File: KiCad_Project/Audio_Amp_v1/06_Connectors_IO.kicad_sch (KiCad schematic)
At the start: 0 parts

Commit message: Updated Power management section, Bluetooth receiver and connectors. Added some components footprints and 3D.
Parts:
- added J1: TS-103-T-A, TS_103_T_A:SAMTEC_TS-103-T-A, symbol TS-103-T-A:TS-103-T-A
- added U2: 2137160001, 2137160001_MOL, symbol USB_C:2137160001
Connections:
- new net: U2.A1 (GND), U2.A12 (GND), U2.B1 (GND), U2.B12 (GND)
- new net: U2.A4 (VBUS), U2.A9 (VBUS), U2.B4 (VBUS), U2.B9 (VBUS)
- new net GNDA: J1.03
- new net UART_RX: J1.02
- new net UART_TX: J1.01

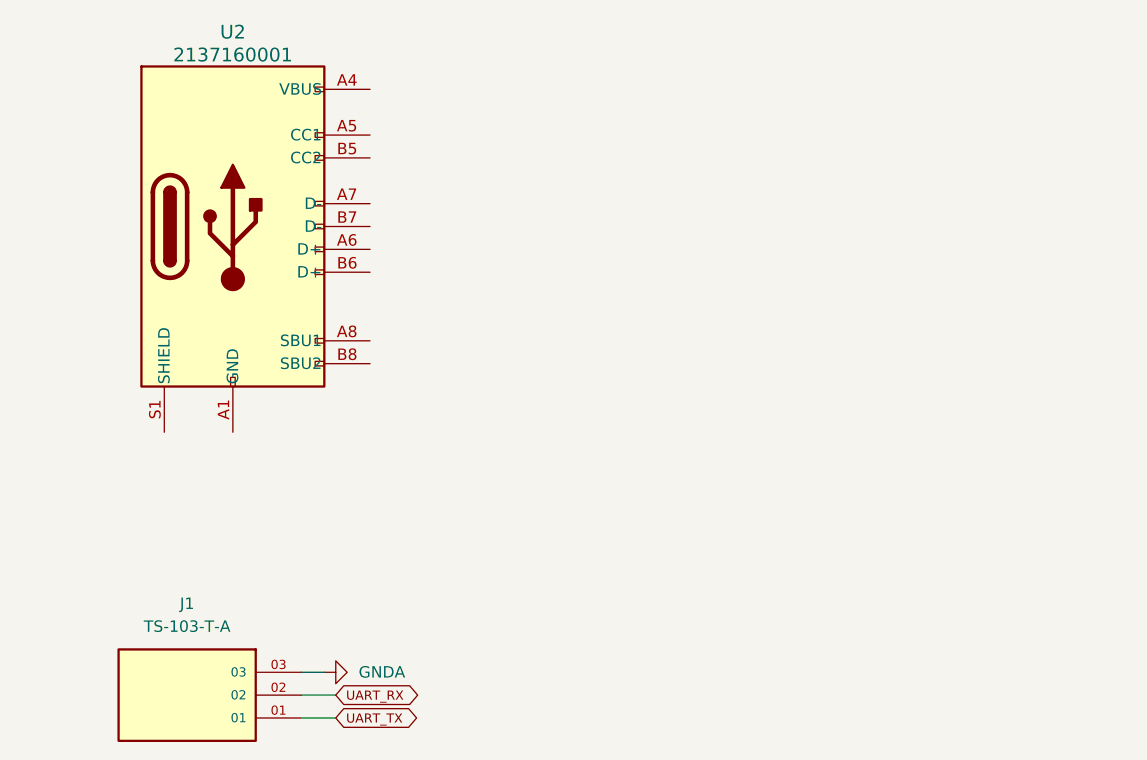
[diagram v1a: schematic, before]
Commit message: Added USB_C schematic and updated the DAC
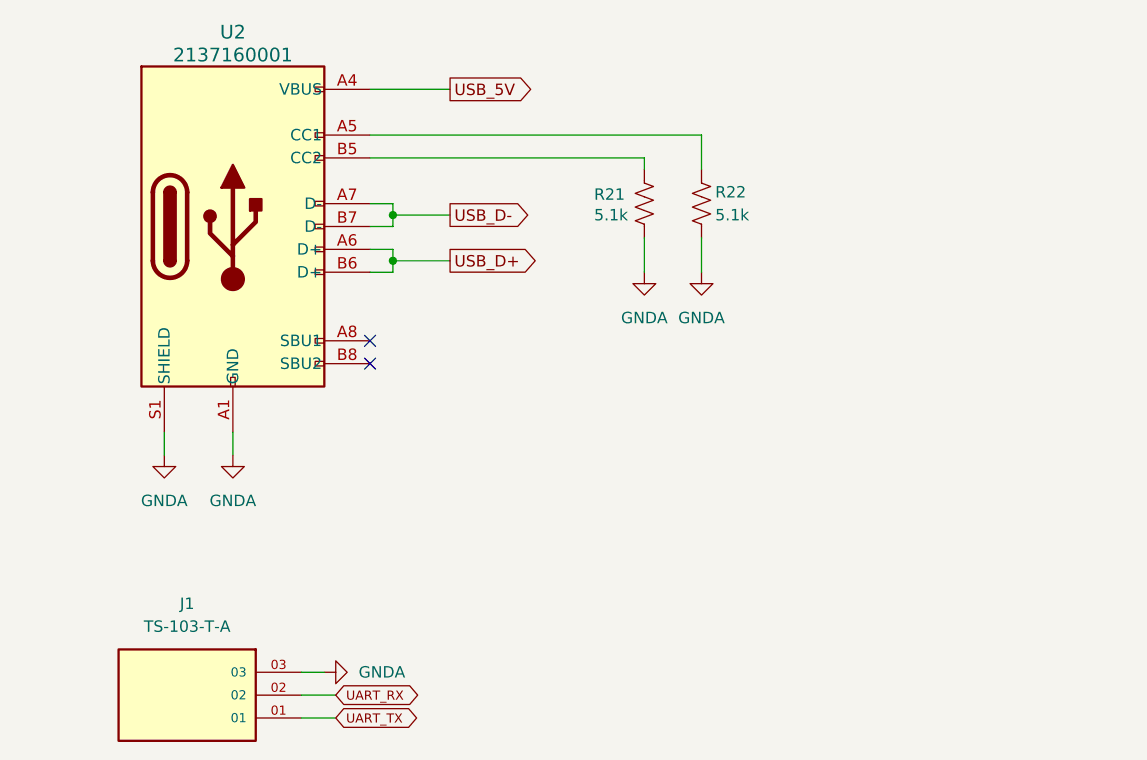
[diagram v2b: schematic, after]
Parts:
- added R21, R22: 5.1k, symbol Device:R_US
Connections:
- net GNDA: now also U2.A1 (GND), U2.A12 (GND), U2.B1 (GND), U2.B12 (GND), U2.S1 (SHIELD), R21.2, R22.2
- net USB_5V: now reaches U2.A4 (VBUS), U2.A9 (VBUS), U2.B4 (VBUS), U2.B9 (VBUS)
- net at U2.A5 (CC1): now also R22.1
- net USB_D+: now reaches U2.A6 (D+)
- net USB_D+: now also U2.B6 (D+)
- net USB_D-: now reaches U2.A7 (D-)
- net USB_D-: now also U2.B7 (D-)
- net at U2.B5 (CC2): now also R21.1
- no-connect marks 0 -> 2

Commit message: Remove KiCad .history from tracking, add to gitignore
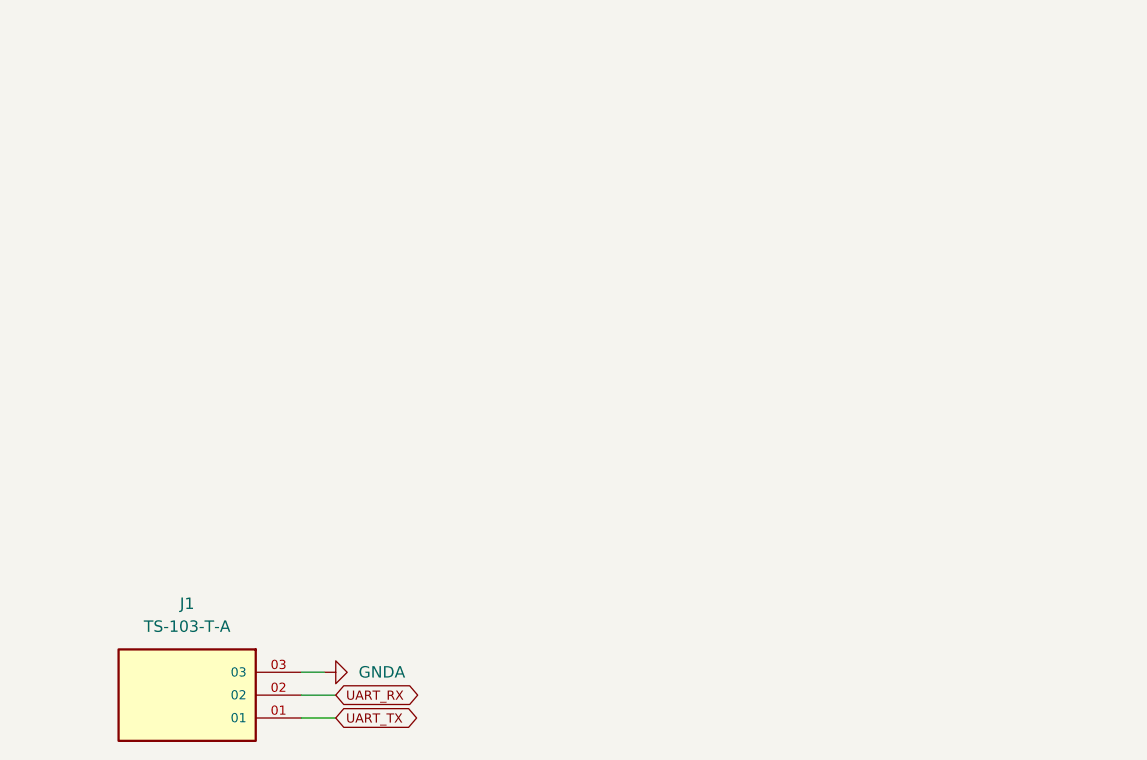
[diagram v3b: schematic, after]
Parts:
- removed R21, R22: 5.1k, symbol Device:R_US
- removed U2: 2137160001, 2137160001_MOL, symbol USB_C:2137160001
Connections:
- no-connect marks 2 -> 0

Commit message: Finished Schematic and started Layout
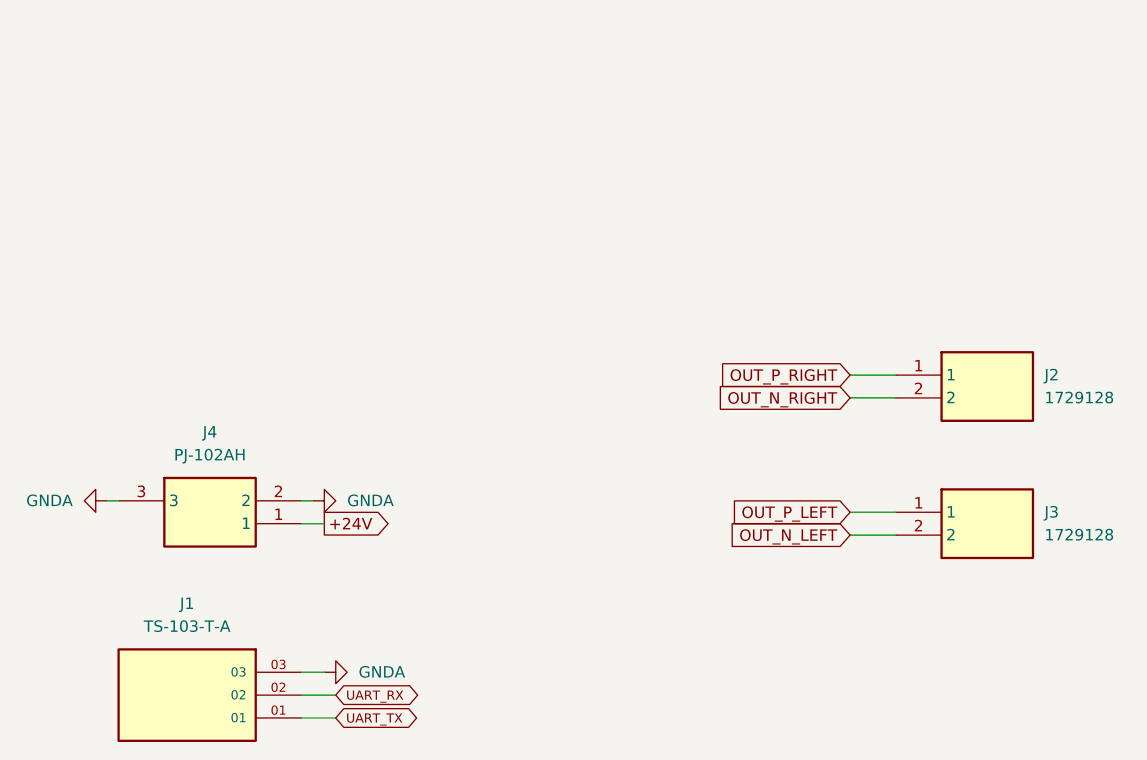
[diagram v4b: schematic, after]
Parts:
- added J2, J3: 1729128, 1729128, symbol 1729128:1729128
- added J4: PJ-102AH, PJ-102AH, symbol PJ-102AH:PJ-102AH
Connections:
- net GNDA: now also J4.2, J4.3
- new net +24V: J4.1
- new net OUT_N_LEFT: J3.2
- new net OUT_N_RIGHT: J2.2
- new net OUT_P_LEFT: J3.1
- new net OUT_P_RIGHT: J2.1

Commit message: Layout Updated, finished routing
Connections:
- net UART_RX: now also J1.01; no longer J1.02
- net UART_TX: now also J1.02; no longer J1.01
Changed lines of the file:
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@@
+		)
+	)
+	(global_label "UART_TX"
+		(shape bidirectional)
+		(at 53.34 116.84 0)
+		(fields_autoplaced yes)
+		(effects
+			(font
+				(size 1.016 1.016)
+			)
+			(justify left)
+		)
+		(property "Intersheetrefs" "${INTERSHEET_REFS}"
+			(at 62.8581 116.84 0)
+			(hide yes)
+			(show_name no)
+			(do_not_autoplace no)
+			(effects
+				(font
+					(size 1.27 1.27)
+				)
+				(justify left)
+			)
 		)
 	)
@@
 	(global_label "UART_RX"
 		(shape bidirectional)
-		(at 53.34 116.84 0)
+		(at 53.34 119.38 0)
 		(fields_autoplaced yes)
 		(effects
@@
 		)
 		(property "Intersheetrefs" "${INTERSHEET_REFS}"
-			(at 63.1 116.84 0)
+			(at 63.1 119.38 0)
 			(hide yes)
 			(show_name no)
@@
 			)
 		)
-	)
-	(global_label "UART_TX"
-		(shape bidirectional)
-		(at 53.34 119.38 0)
-		(fields_autoplaced yes)
-		(effects
-			(font
-				(size 1.016 1.016)
-			)
-			(justify left)
-		)
-		(property "Intersheetrefs" "${INTERSHEET_REFS}"
-			(at 62.8581 119.38 0)
-			(hide yes)
-			(show_name no)
-			(do_not_autoplace no)
-			(effects
-				(font
-					(size 1.27 1.27)
-				)
-				(justify left)
-			)
-		)
